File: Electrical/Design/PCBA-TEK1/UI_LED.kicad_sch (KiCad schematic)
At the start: 36 parts

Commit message: SUKU sync
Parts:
- removed C901, C902, C903, C904, C905: 100n, suku_basics:CAP_0402, symbol suku_basics:CAP
- removed D901, D902, D903, D904, D905: WS2812C-2020, suku_basics:UI_WS2812C-2020, symbol suku_basics:UI_WS2812C-2020
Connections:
- net LED_DATA_IN: now also D906.3 (DIN)
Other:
- note removed: "900"

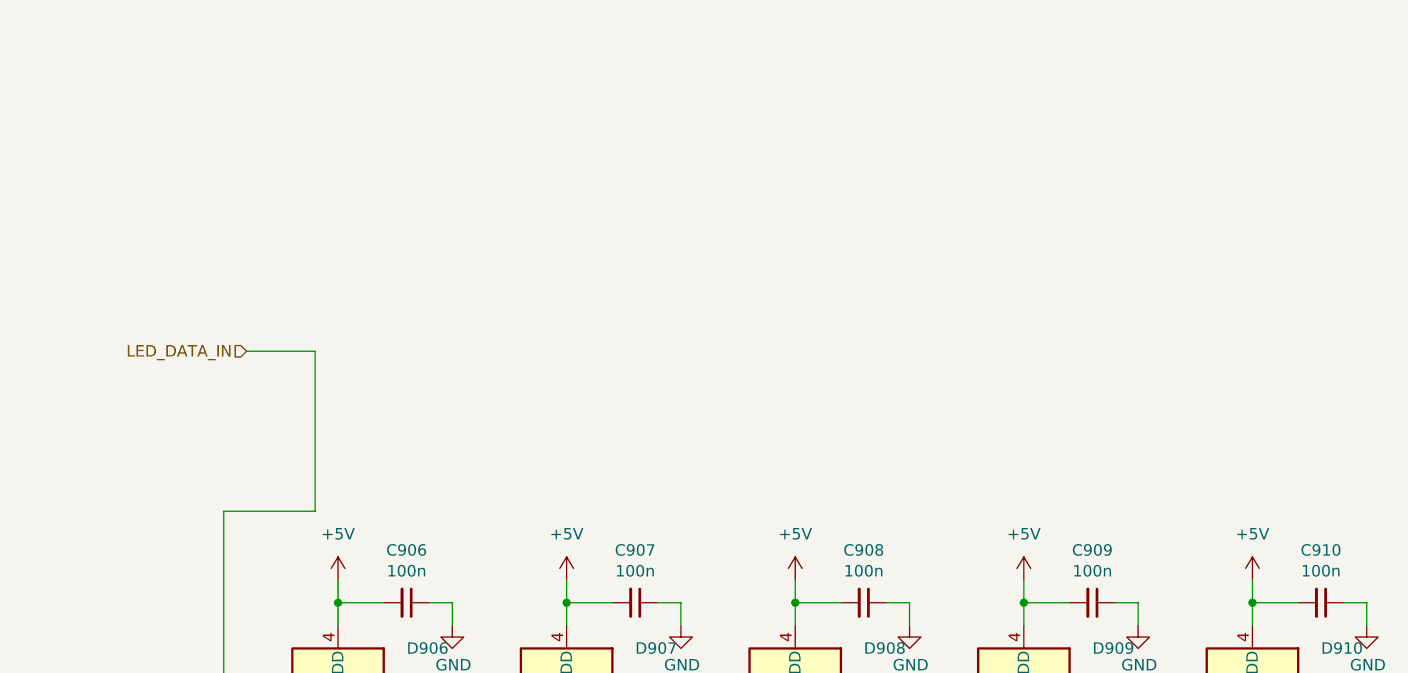
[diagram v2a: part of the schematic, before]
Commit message: SUKU extra led's added for mirrored variant
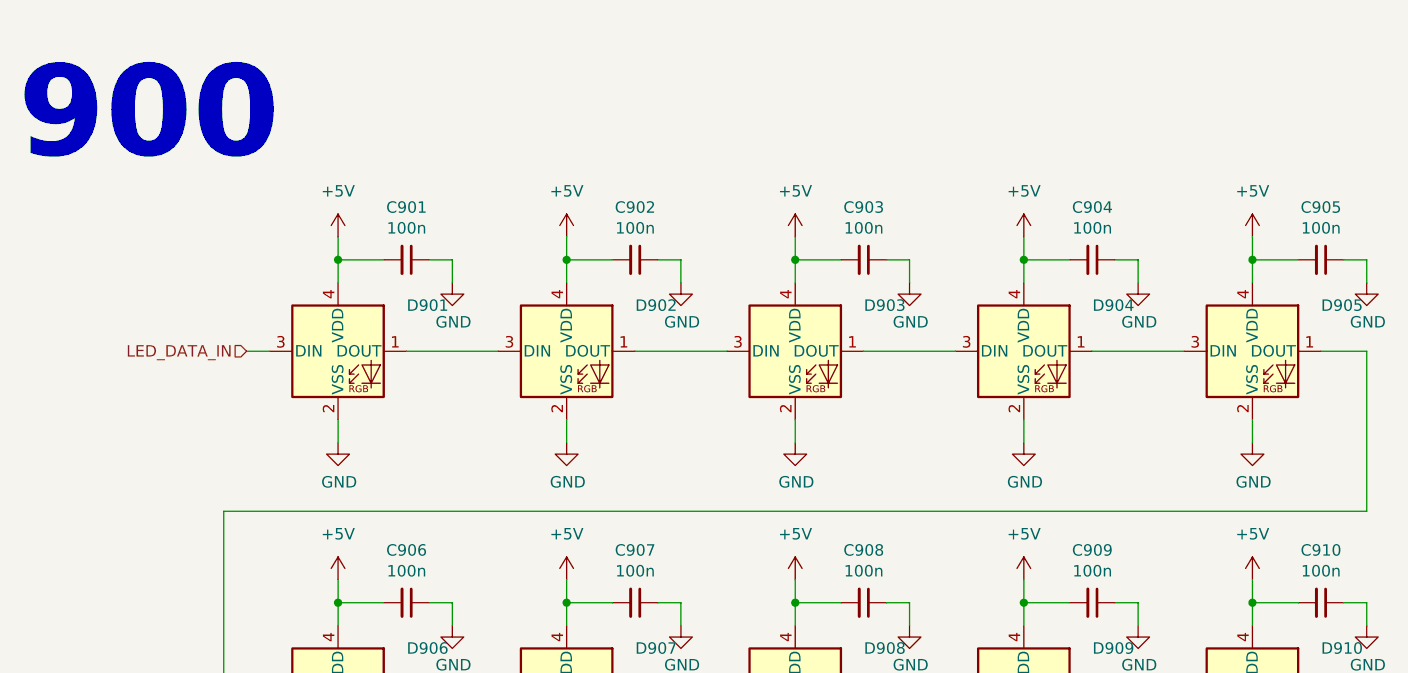
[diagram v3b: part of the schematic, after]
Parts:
- added C901, C902, C903, C904, C905: 100n, suku_basics:CAP_0402, symbol suku_basics:CAP
- added D901, D902, D903, D904, D905: WS2812C-2020, suku_basics:UI_WS2812C-2020, symbol suku_basics:UI_WS2812C-2020
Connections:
- net +5V: now also C901.2, C902.2, C903.2, C904.2, C905.2, D901.4 (VDD), D902.4 (VDD), D903.4 (VDD), D904.4 (VDD), D905.4 (VDD)
- net GND: now also C901.1, C902.1, C903.1, C904.1, C905.1, D901.2 (VSS), D902.2 (VSS), D903.2 (VSS), D904.2 (VSS), D905.2 (VSS)
- net LED_DATA_IN: now also D901.3 (DIN); no longer D906.3 (DIN)
- new net: D905.1 (DOUT), D906.3 (DIN)
- new net: D901.1 (DOUT), D902.3 (DIN)
- new net: D904.1 (DOUT), D905.3 (DIN)
- new net: D903.1 (DOUT), D904.3 (DIN)
- new net: D902.1 (DOUT), D903.3 (DIN)
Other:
- note added: "900"
